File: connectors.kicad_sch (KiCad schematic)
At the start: 65 parts, among them J1 Molex_Nano-Fit_1x2_SMD_105430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, J2 Conn_FAKRA_59S2AQ-40MT5-Z_1, J3 Conn_FAKRA_59S2AQ-40MT5-Z_1, J4 Conn_FAKRA_59S2AQ-40MT5-Z_1, J5 Conn_FAKRA_59S2AQ-40MT5-Z_1, J6 Conn_FFC_WE_68715014522, Q6 DMG1012T-7, U1 SN74LV1T125DBVR, U2 SN74LV1T125DBVR, U8 NTS0102_TSSOP

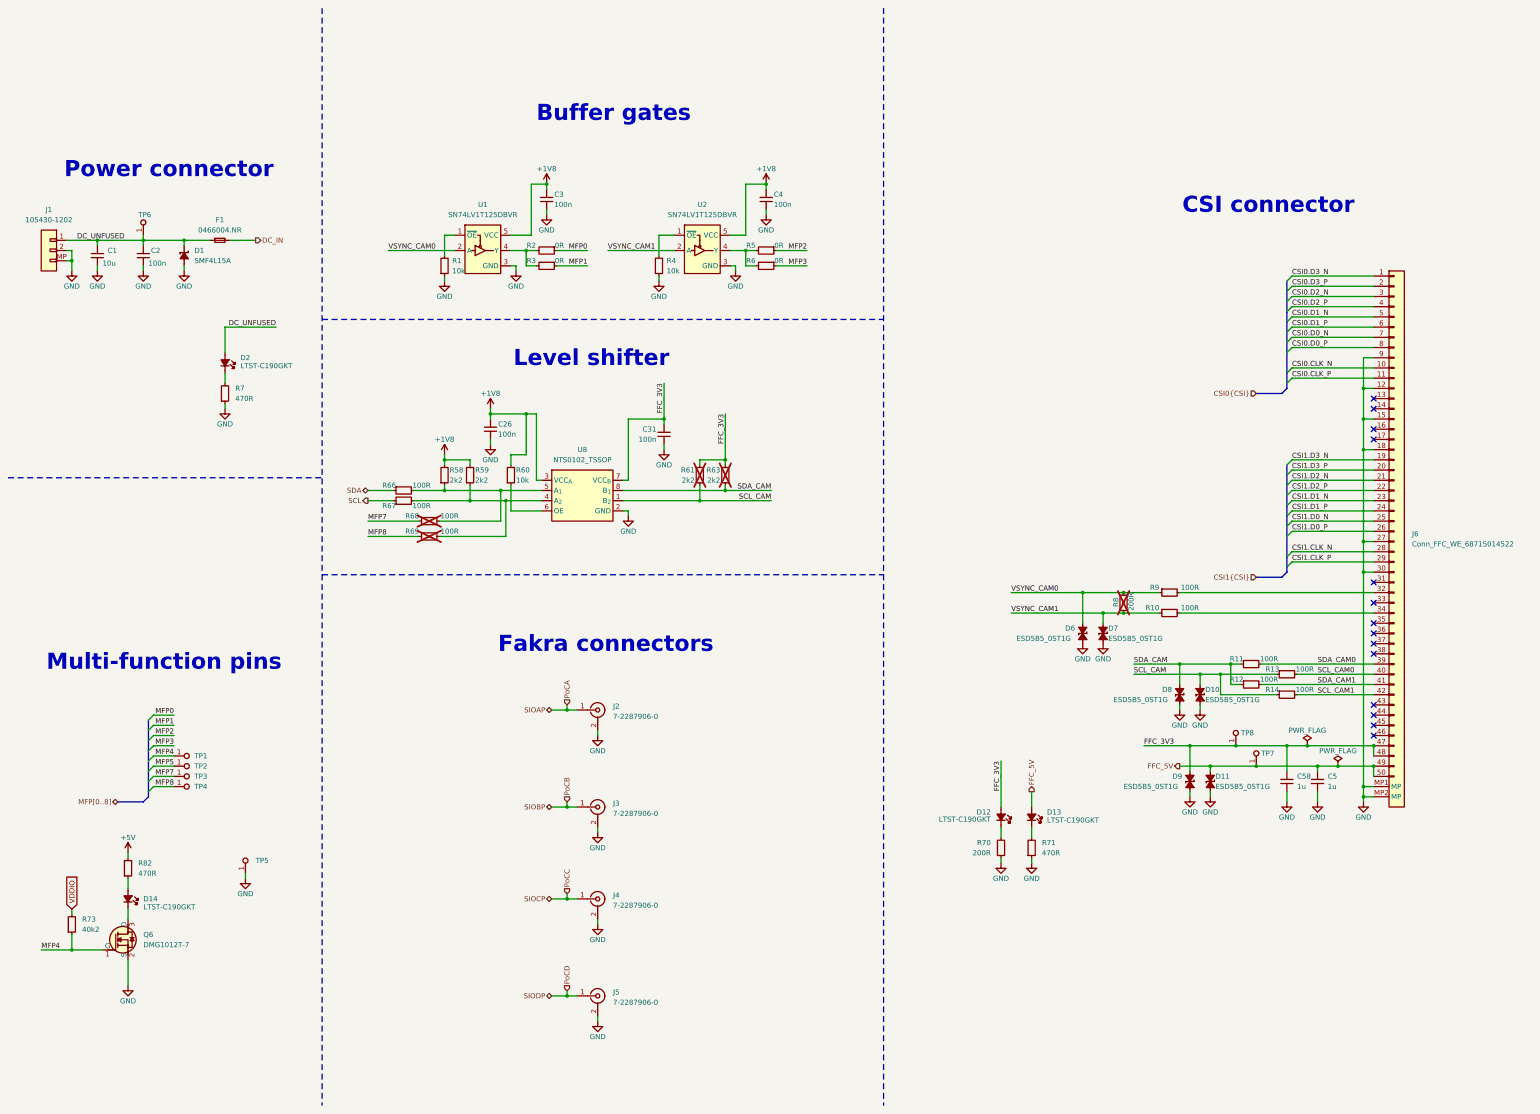
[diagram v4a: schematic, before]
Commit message: [#80515] Add test points on OUT_1V8, 1V8, OUT 1V2, 1V2, 5V, FFC_5V, 12V, OUT_12V, FFC 3V3, DC_IN, DC_UNFUSED SDA, SCL, GND
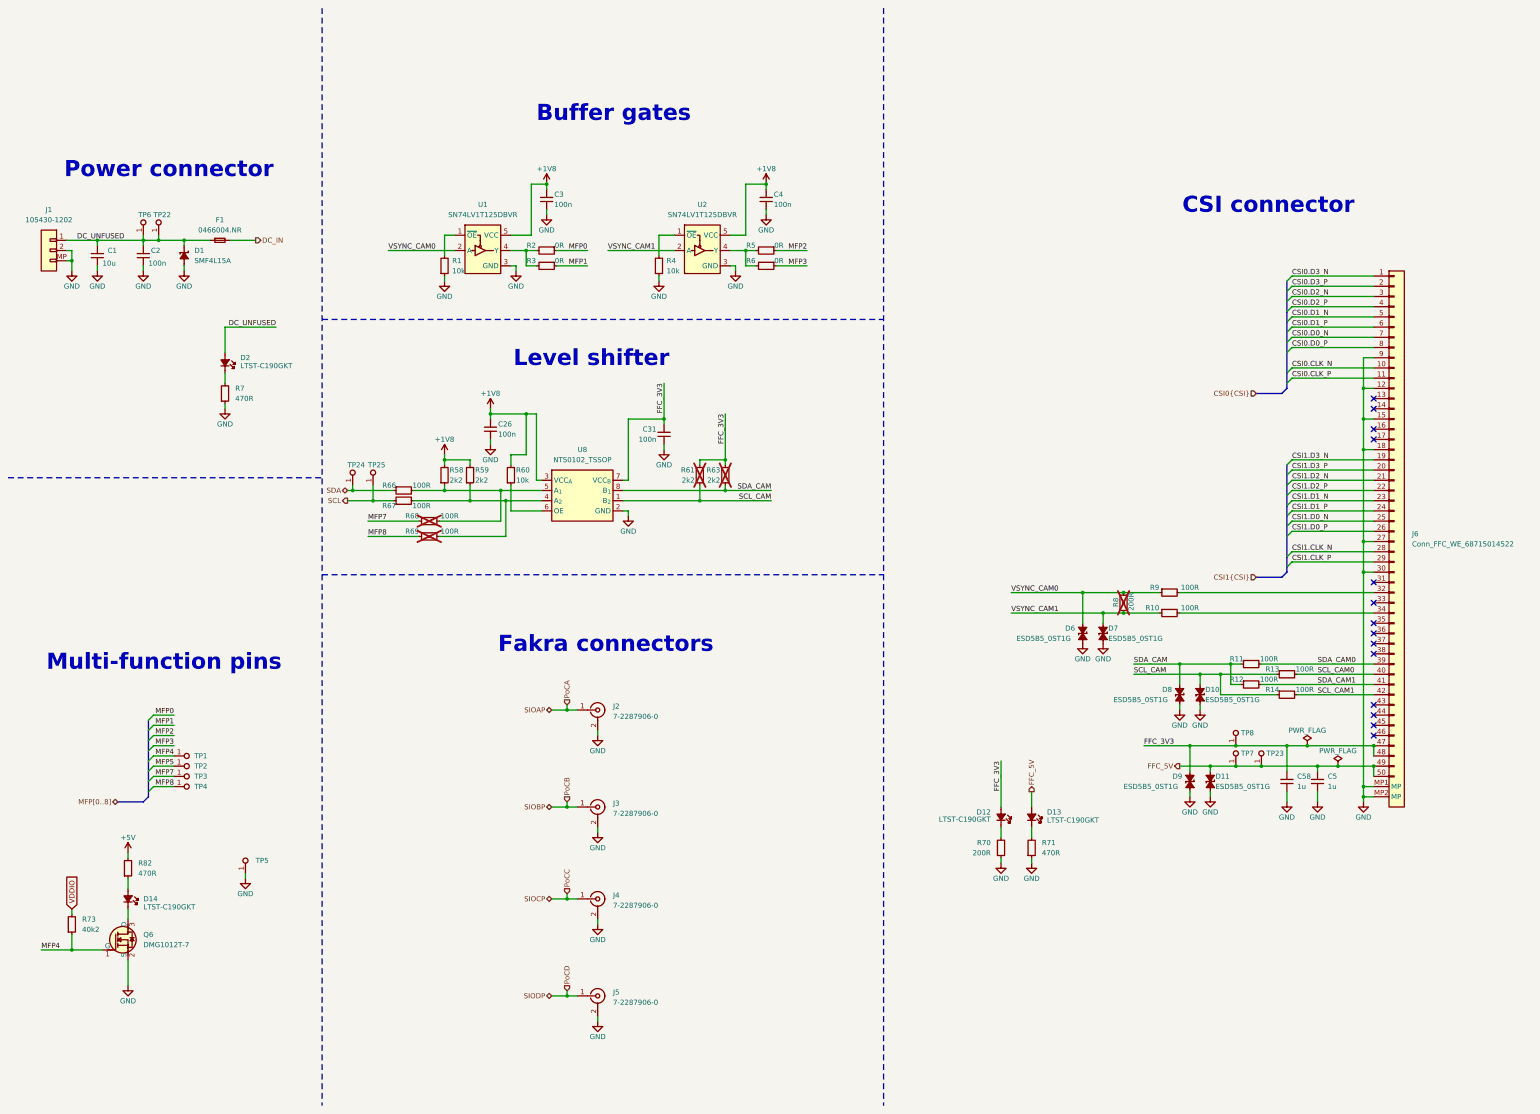
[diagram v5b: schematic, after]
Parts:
- added TP22, TP23, TP24, TP25: TP_0.75mm_SMD, antmicro-footprints:TP_SMD_0.75mm, symbol antmicroTestPoints:TP_0.75mm_SMD
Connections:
- net DC_UNFUSED: now also TP22.1
- net FFC_5V: now also TP23.1
- net SCL: now also TP25.1
- net SDA: now also TP24.1
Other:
- moved on the sheet: TP7
